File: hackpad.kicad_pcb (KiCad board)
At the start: 2 copper layers, 63 x 105 mm, 21 parts, among them J1 Conn_01x04, SW1 SW_Push, SW10 RotaryEncoder_Switch, SW2 SW_Push, SW3 SW_Push, SW4 SW_Push, SW5 SW_Push, SW6 SW_Push, SW7 SW_Push, SW8 SW_Push, SW9 SW_Push, U1 MOUDLE-SEEEDUINO-XIAO

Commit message: PCB: widen board, round corners, add 4 mounting holes
Widened the right edge (board now ~68x105mm, symmetric ~6mm margins)
because the switch grid was only 0.9mm from the original right edge.
Re-applied 4mm rounded corners. Added 4x M2 mounting holes (H1-H4):
top-left, top-right, bottom-left and bottom-center. Bottom-right is
intentionally left open (rotary encoder) — the case will get a support
boss under the encoder instead.

Co-Authored-By: Claude Opus 4.8 <noreply@anthropic.com>
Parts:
- added H1: MountingHole_2.2mm_M2, MountingHole:MountingHole_2.2mm_M2, F.Cu at (18.0, 18.0)
- added H2: MountingHole_2.2mm_M2, MountingHole:MountingHole_2.2mm_M2, F.Cu at (79.0, 18.0)
- added H3: MountingHole_2.2mm_M2, MountingHole:MountingHole_2.2mm_M2, F.Cu at (18.0, 115.0)
- added H4: MountingHole_2.2mm_M2, MountingHole:MountingHole_2.2mm_M2, F.Cu at (48.5, 115.0)
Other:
- board size 63 x 105 mm -> 68 x 105 mm

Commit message: PCB: add GND copper pour on both layers
Filled F.Cu + B.Cu with a GND zone (thermal reliefs, remove islands).
Set the encoder common pad (SW10 pad C) to a solid zone connection to
clear a starved-thermal DRC error. DRC now clean apart from intentional
diode-under-switch courtyard overlaps and cosmetic silk warnings.

Co-Authored-By: Claude Opus 4.8 <noreply@anthropic.com>
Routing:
- added copper zone on B.Cu, net /GND
- added copper zone on F.Cu, net /GND
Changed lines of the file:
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@@
 		)
 	)
+	(footprint "MountingHole:MountingHole_2.2mm_M2"
+		(layer "F.Cu")
+		(at 79 18)
+		(property "Reference" "H2"
+			(at 0 -3 0)
+			(layer "F.SilkS")
+			(effects
+				(font
+					(size 1 1)
+					(thickness 0.15)
+				)
+			)
+		)
+		(property "Value" "MountingHole_2.2mm_M2"
+			(at 0 3 0)
+			(layer "F.Fab")
+			(effects
+				(font
+					(size 1 1)
+					(thickness 0.15)
+				)
+			)
+		)
+		(property "Datasheet" ""
+			(at 0 0 0)
+			(layer "F.Fab")
+			(hide yes)
+			(effects
+				(font
+					(size 1.27 1.27)
+				)
+			)
+		)
+		(property "Description" ""
+			(at 0 0 0)
+			(layer "F.Fab")
+			(hide yes)
+			(effects
+				(font
+					(size 1.27 1.27)
+				)
+			)
+		)
+		(attr exclude_from_pos_files exclude_from_bom allow_missing_courtyard)
+		(duplicate_pad_numbers_are_jumpers no)
+		(pad "" np_thru_hole circle
+			(at 0 0)
+			(size 2.2 2.2)
+			(drill 2.2)
+			(layers "*.Cu" "*.Mask")
+		)
+		(embedded_fonts no)
+	)
+	(footprint "MountingHole:MountingHole_2.2mm_M2"
+		(layer "F.Cu")
+		(at 48.49 115)
+		(property "Reference" "H4"
+			(at 0 -3 0)
+			(layer "F.SilkS")
+			(effects
+				(font
+					(size 1 1)
+					(thickness 0.15)
+				)
+			)
+		)
+		(property "Value" "MountingHole_2.2mm_M2"
+			(at 0 3 0)
+			(layer "F.Fab")
+			(effects
+				(font
+					(size 1 1)
+					(thickness 0.15)
+				)
+			)
+		)
+		(property "Datasheet" ""
+			(at 0 0 0)
+			(layer "F.Fab")
+			(hide yes)
+			(effects
+				(font
+					(size 1.27 1.27)
+				)
+			)
+		)
+		(property "Description" ""
+			(at 0 0 0)
+			(layer "F.Fab")
+			(hide yes)
+			(effects
+				(font
+					(size 1.27 1.27)
+				)
+			)
+		)
+		(attr exclude_from_pos_files exclude_from_bom allow_missing_courtyard)
+		(duplicate_pad_numbers_are_jumpers no)
+		(pad "" np_thru_hole circle
+			(at 0 0)
+			(size 2.2 2.2)
+			(drill 2.2)
+			(layers "*.Cu" "*.Mask")
+		)
+		(embedded_fonts no)
+	)
 	(footprint "Connector_PinHeader_2.54mm:PinHeader_1x04_P2.54mm_Vertical"
 		(layer "F.Cu")
@@
 		)
 	)
+	(footprint "MountingHole:MountingHole_2.2mm_M2"
+		(layer "F.Cu")
+		(at 18 115)
+		(property "Reference" "H3"
+			(at 0 -3 0)
+			(layer "F.SilkS")
+			(effects
+				(font
+					(size 1 1)
+					(thickness 0.15)
+				)
+			)
+		)
+		(property "Value" "MountingHole_2.2mm_M2"
+			(at 0 3 0)
+			(layer "F.Fab")
+			(effects
+				(font
+					(size 1 1)
+					(thickness 0.15)
+				)
+			)
+		)
+		(property "Datasheet" ""
+			(at 0 0 0)
+			(layer "F.Fab")
+			(hide yes)
+			(effects
+				(font
+					(size 1.27 1.27)
+				)
+			)
+		)
+		(property "Description" ""
+			(at 0 0 0)
+			(layer "F.Fab")
+			(hide yes)
+			(effects
+				(font
+					(size 1.27 1.27)
+				)
+			)
+		)
+		(attr exclude_from_pos_files exclude_from_bom allow_missing_courtyard)
+		(duplicate_pad_numbers_are_jumpers no)
+		(pad "" np_thru_hole circle
+			(at 0 0)
+			(size 2.2 2.2)
+			(drill 2.2)
+			(layers "*.Cu" "*.Mask")
+		)
+		(embedded_fonts no)
+	)
 	(footprint "Button_Switch_Keyboard:SW_Cherry_MX_1.00u_PCB"
 		(layer "F.Cu")
@@
 		)
 	)
+	(footprint "MountingHole:MountingHole_2.2mm_M2"
+		(layer "F.Cu")
+		(at 18 18)
+		(property "Reference" "H1"
+			(at 0 -3 0)
+			(layer "F.SilkS")
+			(effects
+				(font
+					(size 1 1)
+					(thickness 0.15)
+				)
+			)
+		)
+		(property "Value" "MountingHole_2.2mm_M2"
+			(at 0 3 0)
+			(layer "F.Fab")
+			(effects
+				(font
+					(size 1 1)
+					(thickness 0.15)
+				)
+			)
+		)
+		(property "Datasheet" ""
+			(at 0 0 0)
+			(layer "F.Fab")
+			(hide yes)
+			(effects
+				(font
+					(size 1.27 1.27)
+				)
+			)
+		)
+		(property "Description" ""
+			(at 0 0 0)
+			(layer "F.Fab")
+			(hide yes)
+			(effects
+				(font
+					(size 1.27 1.27)
+				)
+			)
+		)
+		(attr exclude_from_pos_files exclude_from_bom allow_missing_courtyard)
+		(duplicate_pad_numbers_are_jumpers no)
+		(pad "" np_thru_hole circle
+			(at 0 0)
+			(size 2.2 2.2)
+			(drill 2.2)
+			(layers "*.Cu" "*.Mask")
+		)
+		(embedded_fonts no)
+	)
 	(footprint "Footprints-für-hackpad:XIAO-Generic-Hybrid-14P-2.54-21X17.8MM"
 		(layer "F.Cu")
@@
 			(pinfunction "C_C")
 			(pintype "passive")
+			(zone_connect 2)
 		)
 		(pad "MP" thru_hole rect
@@
 		(layer "Cmts.User")
 	)
-	(gr_line
-		(start 18.49 13.82)
-		(end 78.49 13.82)
+	(gr_arc
+		(start 14.49 17.82)
+		(mid 15.661573 14.991573)
+		(end 18.49 13.82)
 		(stroke
 			(width 0.05)
@@
 		(layer "Edge.Cuts")
 	)
-	(gr_arc
-		(start 78.49 13.82)
-		(mid 81.318427 14.991573)
-		(end 82.49 17.82)
+	(gr_line
+		(start 14.49 114.82)
+		(end 14.49 17.82)
 		(stroke
 			(width 0.05)
@@
 	)
 	(gr_line
-		(start 82.49 17.82)
-		(end 82.49 114.82)
+		(start 18.49 13.82)
+		(end 78.49 13.82)
 		(stroke
 			(width 0.05)
@@
 	)
 	(gr_arc
-		(start 82.49 114.82)
-		(mid 81.318427 117.648427)
-		(end 78.49 118.82)
+		(start 18.49 118.82)
+		(mid 15.661573 117.648427)
+		(end 14.49 114.82)
 		(stroke
 			(width 0.05)
@@
 		(layer "Edge.Cuts")
 	)
-	(gr_line
-		(start 78.49 118.82)
-		(end 18.49 118.82)
+	(gr_arc
+		(start 78.49 13.82)
+		(mid 81.318427 14.991573)
+		(end 82.49 17.82)
 		(stroke
 			(width 0.05)
@@
 		(layer "Edge.Cuts")
 	)
-	(gr_arc
-		(start 18.49 118.82)
-		(mid 15.661573 117.648427)
-		(end 14.49 114.82)
+	(gr_line
+		(start 78.49 118.82)
+		(end 18.49 118.82)
 		(stroke
 			(width 0.05)
@@
 	)
 	(gr_line
-		(start 14.49 114.82)
-		(end 14.49 17.82)
+		(start 82.49 17.82)
+		(end 82.49 114.82)
 		(stroke
 			(width 0.05)
@@
 	)
 	(gr_arc
-		(start 14.49 17.82)
-		(mid 15.661573 14.991573)
-		(end 18.49 13.82)
+		(start 82.49 114.82)
+		(mid 81.318427 117.648427)
+		(end 78.49 118.82)
 		(stroke
 			(width 0.05)
@@
 		(layer "Edge.Cuts")
 	)
-	(footprint "MountingHole:MountingHole_2.2mm_M2"
-		(layer "F.Cu")
-		(at 18.0 18.0)
-		(attr exclude_from_pos_files exclude_from_bom allow_missing_courtyard)
-		(property "Reference" "H1"
-			(at 0 -3 0)
-			(layer "F.SilkS")
-			(effects
-				(font
-					(size 1 1)
-					(thickness 0.15)
-				)
-			)
-		)
-		(property "Value" "MountingHole_2.2mm_M2"
-			(at 0 3 0)
-			(layer "F.Fab")
-			(effects
-				(font
-					(size 1 1)
-					(thickness 0.15)
-				)
-			)
-		)
-		(pad "" np_thru_hole circle
-			(at 0 0)
-			(size 2.2 2.2)
-			(drill 2.2)
-			(layers "*.Cu" "*.Mask")
-		)
-	)
-	(footprint "MountingHole:MountingHole_2.2mm_M2"
-		(layer "F.Cu")
-		(at 79.0 18.0)
-		(attr exclude_from_pos_files exclude_from_bom allow_missing_courtyard)
-		(property "Reference" "H2"
-			(at 0 -3 0)
-			(layer "F.SilkS")
-			(effects
-				(font
-					(size 1 1)
-					(thickness 0.15)
-				)
-			)
-		)
-		(property "Value" "MountingHole_2.2mm_M2"
-			(at 0 3 0)
-			(layer "F.Fab")
-			(effects
-				(font
-					(size 1 1)
-					(thickness 0.15)
-				)
-			)
-		)
-		(pad "" np_thru_hole circle
-			(at 0 0)
-			(size 2.2 2.2)
-			(drill 2.2)
-			(layers "*.Cu" "*.Mask")
-		)
-	)
-	(footprint "MountingHole:MountingHole_2.2mm_M2"
-		(layer "F.Cu")
-		(at 18.0 115.0)
-		(attr exclude_from_pos_files exclude_from_bom allow_missing_courtyard)
-		(property "Reference" "H3"
-			(at 0 -3 0)
-			(layer "F.SilkS")
-			(effects
-				(font
-					(size 1 1)
-					(thickness 0.15)
-				)
-			)
-		)
-		(property "Value" "MountingHole_2.2mm_M2"
-			(at 0 3 0)
-			(layer "F.Fab")
-			(effects
-				(font
-					(size 1 1)
-					(thickness 0.15)
-				)
-			)
-		)
-		(pad "" np_thru_hole circle
-			(at 0 0)
-			(size 2.2 2.2)
-			(drill 2.2)
-			(layers "*.Cu" "*.Mask")
-		)
-	)
-	(footprint "MountingHole:MountingHole_2.2mm_M2"
-		(layer "F.Cu")
-		(at 48.49 115.0)
-		(attr exclude_from_pos_files exclude_from_bom allow_missing_courtyard)
-		(property "Reference" "H4"
-			(at 0 -3 0)
-			(layer "F.SilkS")
-			(effects
-				(font
-					(size 1 1)
-					(thickness 0.15)
-				)
-			)
-		)
-		(property "Value" "MountingHole_2.2mm_M2"
-			(at 0 3 0)
-			(layer "F.Fab")
-			(effects
-				(font
-					(size 1 1)
-					(thickness 0.15)
-				)
-			)
-		)
-		(pad "" np_thru_hole circle
-			(at 0 0)
-			(size 2.2 2.2)
-			(drill 2.2)
-			(layers "*.Cu" "*.Mask")
-		)
-	)
 	(segment
 		(start 29.49 46.82)
@@
 		(net "Net-(D1-A)")
 	)
+	(zone
+		(net "/GND")
+		(layers "F.Cu" "B.Cu")
+		(hatch edge 0.5)
+		(connect_pads
+			(clearance 0.5)
+		)
+		(min_thickness 0.25)
+		(fill yes
+			(thermal_gap 0.5)
+			(thermal_bridge_width 0.5)
+			(island_removal_mode 0)
+		)
+		(polygon
+			(pts
+				(xy 34.5 119) (xy 47.5 119) (xy 83.073345 119.703523) (xy 82.193881 12.938263) (xy 14 13.5) (xy 13.59916 74.370272)
+				(xy 14.051924 119.165151)
+			)
+		)
+	)
 	(embedded_fonts no)

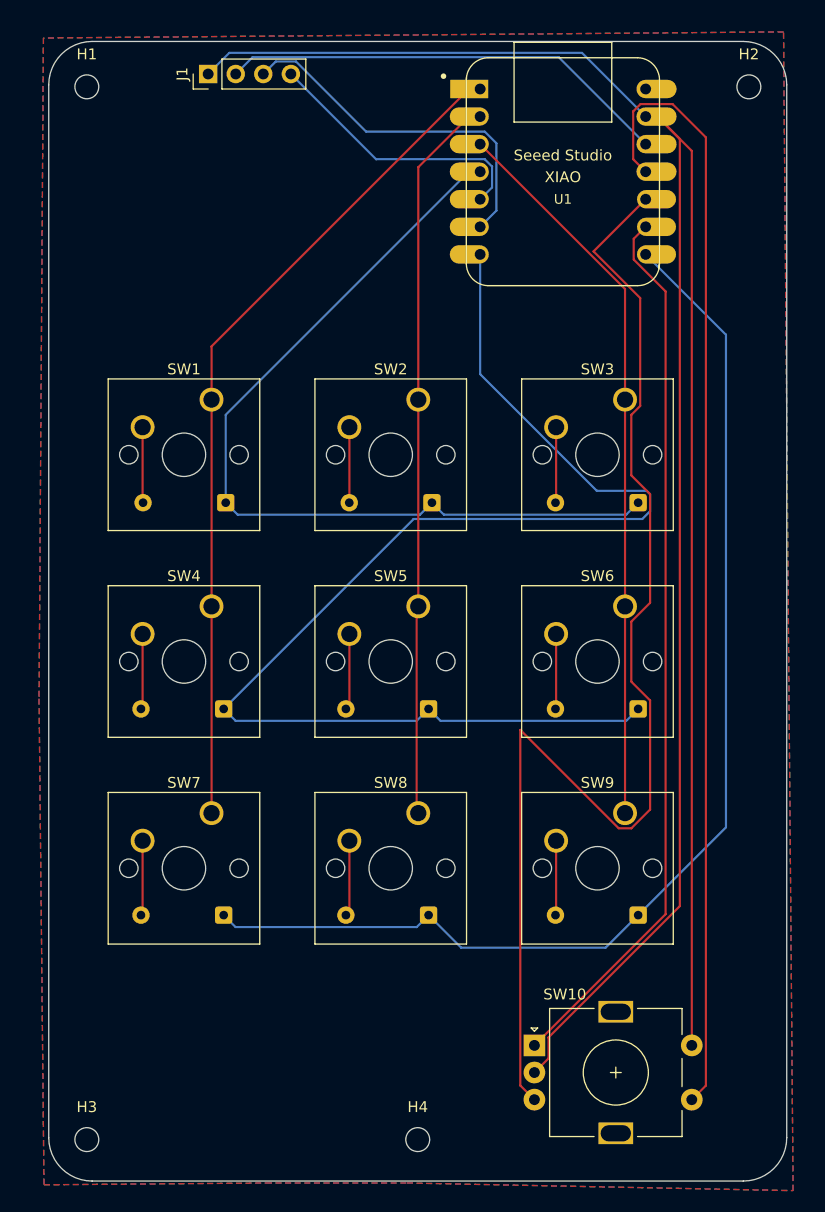
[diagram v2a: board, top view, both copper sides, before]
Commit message: Resize PCB under 100mm, finalize case STL, document AI usage
- PCB outline trimmed to 68 x 99.68 mm (Stardance <100x100 limit);
  top mounting holes untouched, bottom edge + bottom holes moved up
- Update STEP export to match resized board
- Replace separate case parts with final combined STL (tray + open
  top frame, no-supports, PCB anti-flex support grid)
- README: sync status checklist, new dimensions, add transparent
  "Use of AI" section (hardware by hand; AI assisted on firmware/app)

Co-Authored-By: Claude Opus 4.8 <noreply@anthropic.com>
Claude-Session: https://claude.ai/code/session_01VPvtJRWkd5XUxsE6SwSzo5
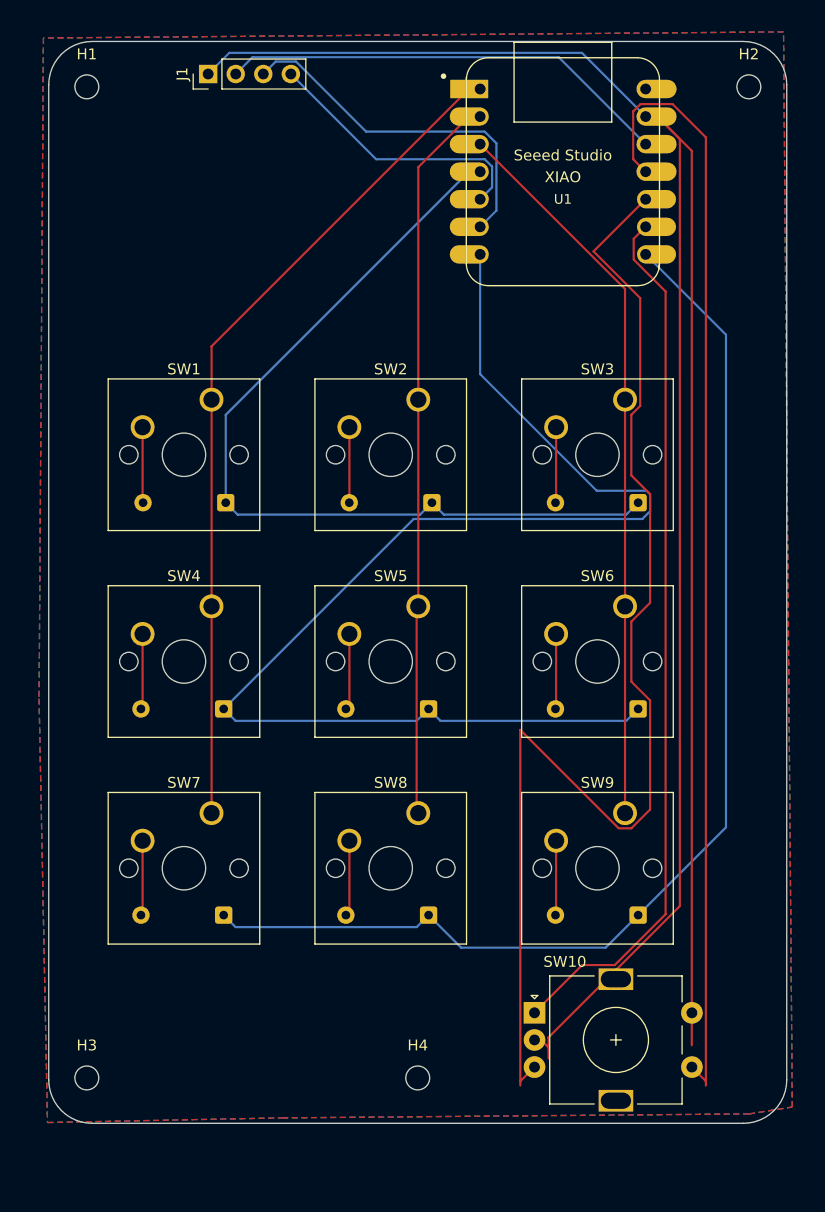
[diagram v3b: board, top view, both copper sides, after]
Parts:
- moved H3 5.68 mm to (18.0, 109.3)
- moved H4 5.68 mm to (48.5, 109.3)
- moved SW10 3.00 mm to (59.2, 103.3)
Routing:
- net /ENC_A: track 82.1 -> 80.9 mm
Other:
- board size 68 x 105 mm -> 68 x 99.7 mm
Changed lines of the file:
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@@
 	(footprint "MountingHole:MountingHole_2.2mm_M2"
 		(layer "F.Cu")
-		(at 48.49 115)
+		(at 48.49 109.32)
 		(property "Reference" "H4"
 			(at 0 -3 0)
@@
 	(footprint "MountingHole:MountingHole_2.2mm_M2"
 		(layer "F.Cu")
-		(at 18 115)
+		(at 18 109.32)
 		(property "Reference" "H3"
 			(at 0 -3 0)
@@
 	(footprint "Rotary_Encoder:RotaryEncoder_Alps_EC11E-Switch_Vertical_H20mm"
 		(layer "F.Cu")
-		(at 59.24 106.32)
+		(at 59.25 103.32)
 		(descr "Alps rotary encoder, EC11E... with switch, vertical shaft, http://www.alps.com/prod/info/E/HTML/Encoder/Incremental/EC11/EC11E15204A3.html")
 		(tags "rotary encoder")
@@
 	)
 	(gr_line
-		(start 14.49 114.82)
+		(start 14.49 109.5)
 		(end 14.49 17.82)
 		(stroke
@@
 	)
 	(gr_arc
-		(start 18.49 118.82)
-		(mid 15.661573 117.648427)
-		(end 14.49 114.82)
+		(start 18.49 113.5)
+		(mid 15.661573 112.328427)
+		(end 14.49 109.5)
 		(stroke
 			(width 0.05)
@@
 	)
 	(gr_line
-		(start 78.49 118.82)
-		(end 18.49 118.82)
+		(start 78.49 113.5)
+		(end 18.49 113.5)
 		(stroke
 			(width 0.05)
@@
 	(gr_line
 		(start 82.49 17.82)
-		(end 82.49 114.82)
+		(end 82.49 109.5)
 		(stroke
 			(width 0.05)
@@
 	)
 	(gr_arc
-		(start 82.49 114.82)
-		(mid 81.318427 117.648427)
-		(end 78.49 118.82)
+		(start 82.49 109.5)
+		(mid 81.318427 112.328427)
+		(end 78.49 113.5)
 		(stroke
 			(width 0.05)
@@
 	)
 	(segment
+		(start 60.54 107.52)
+		(end 60.54 106.5)
+		(width 0.2)
+		(layer "F.Cu")
+		(net "/GND")
+	)
+	(segment
 		(start 70.576346 20.74)
 		(end 69.49 20.74)
@@
 	)
 	(segment
-		(start 59.24 108.82)
-		(end 60.54 107.52)
+		(start 59.24 105.82)
+		(end 59.86 105.82)
+		(width 0.2)
+		(layer "F.Cu")
+		(net "/GND")
+	)
+	(segment
+		(start 59.86 105.82)
+		(end 60.54 106.5)
 		(width 0.2)
 		(layer "F.Cu")
@@
 	)
 	(segment
-		(start 60.54 107.52)
+		(start 60.54 106.5)
 		(end 60.54 105.585686)
 		(width 0.2)
@@
 	)
 	(segment
-		(start 59.24 106.32)
-		(end 71.33 94.23)
+		(start 68.39 32)
+		(end 69.49 30.9)
 		(width 0.2)
 		(layer "F.Cu")
@@
 	)
 	(segment
-		(start 68.39 32)
-		(end 69.49 30.9)
+		(start 59.24 103.32)
+		(end 63.64 98.92)
+		(width 0.2)
+		(layer "F.Cu")
+		(net "/ENC_A")
+	)
+	(segment
+		(start 63.64 98.92)
+		(end 66.64 98.92)
 		(width 0.2)
 		(layer "F.Cu")
@@
 	)
 	(segment
+		(start 66.64 98.92)
+		(end 71.33 94.23)
+		(width 0.2)
+		(layer "F.Cu")
+		(net "/ENC_A")
+	)
+	(segment
 		(start 68.169899 86.32)
 		(end 69.9 84.589899)
@@
 	)
 	(segment
+		(start 59.24 108.32)
+		(end 57.94 109.62)
+		(width 0.2)
+		(layer "F.Cu")
+		(net "/ENC_B")
+	)
+	(segment
 		(start 68.169899 53.805155)
 		(end 68.169899 48.22)
@@
 	)
 	(segment
-		(start 59.24 111.32)
-		(end 57.94 110.02)
+		(start 57.94 110.02)
+		(end 57.94 109.62)
 		(width 0.2)
 		(layer "F.Cu")
@@
 	)
 	(segment
-		(start 57.94 110.02)
+		(start 57.94 109.62)
 		(end 57.94 77.249899)
 		(width 0.2)
@@
 	)
 	(segment
-		(start 73.74 111.32)
-		(end 75.04 110.02)
+		(start 68.34 20.263654)
+		(end 68.34 24.67)
 		(width 0.2)
 		(layer "F.Cu")
@@
 	)
 	(segment
-		(start 68.34 20.263654)
-		(end 68.34 24.67)
+		(start 73.74 108.32)
+		(end 75.04 109.62)
+		(width 0.2)
+		(layer "F.Cu")
+		(net "/ENC_SW")
+	)
+	(segment
+		(start 75.04 110.02)
+		(end 75.04 109.62)
 		(width 0.2)
 		(layer "F.Cu")
@@
 	)
 	(segment
-		(start 75.04 110.02)
+		(start 75.04 109.62)
 		(end 75.04 22.663654)
 		(width 0.2)
@@
 		(polygon
 			(pts
-				(xy 34.5 119) (xy 47.5 119) (xy 83.073345 119.703523) (xy 82.193881 12.938263) (xy 14 13.5) (xy 13.59916 74.370272)
-				(xy 14.051924 119.165151)
+				(xy 36 113) (xy 79.02495 112.633974) (xy 83 112) (xy 82.193881 12.938263) (xy 14 13.5) (xy 13.59916 74.370272)
+				(xy 14.375777 113.429951)
 			)
 		)
